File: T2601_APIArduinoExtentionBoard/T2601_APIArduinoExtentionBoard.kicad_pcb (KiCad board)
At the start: 2 copper layers, 60 x 90 mm, 75 parts, among them J1 Conn_01x10_Socket, J11 Conn_01x04_Pin, J12 Screw_Terminal_01x02, J13 Conn_01x04_Pin, J14 Screw_Terminal_01x02, J15 Conn_02x08_Counter_Clockwise, J2 Conn_01x10_Socket, J3 Conn_01x10_Socket, J4 Conn_01x10_Socket, J5 Screw_Terminal_01x08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

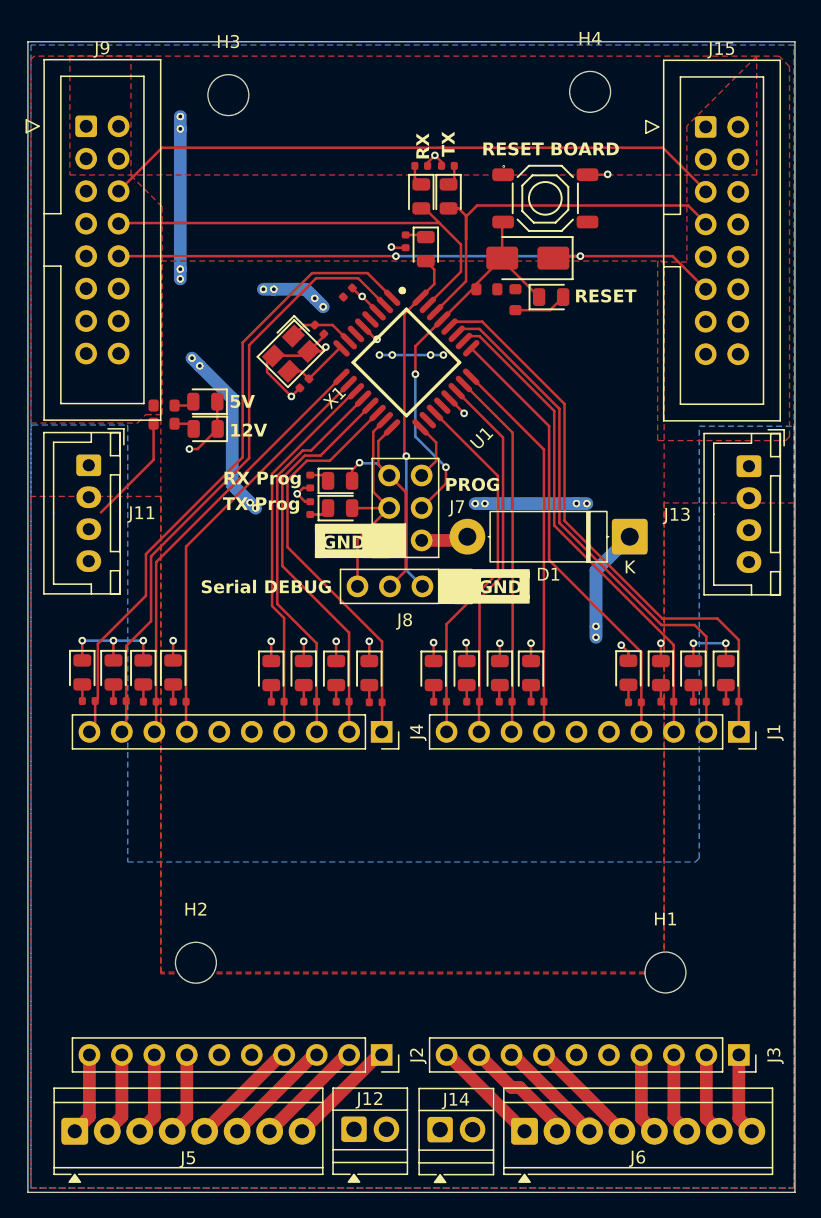
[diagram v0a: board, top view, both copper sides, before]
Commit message: V0.5 - Mounting Hole + Silkscreen
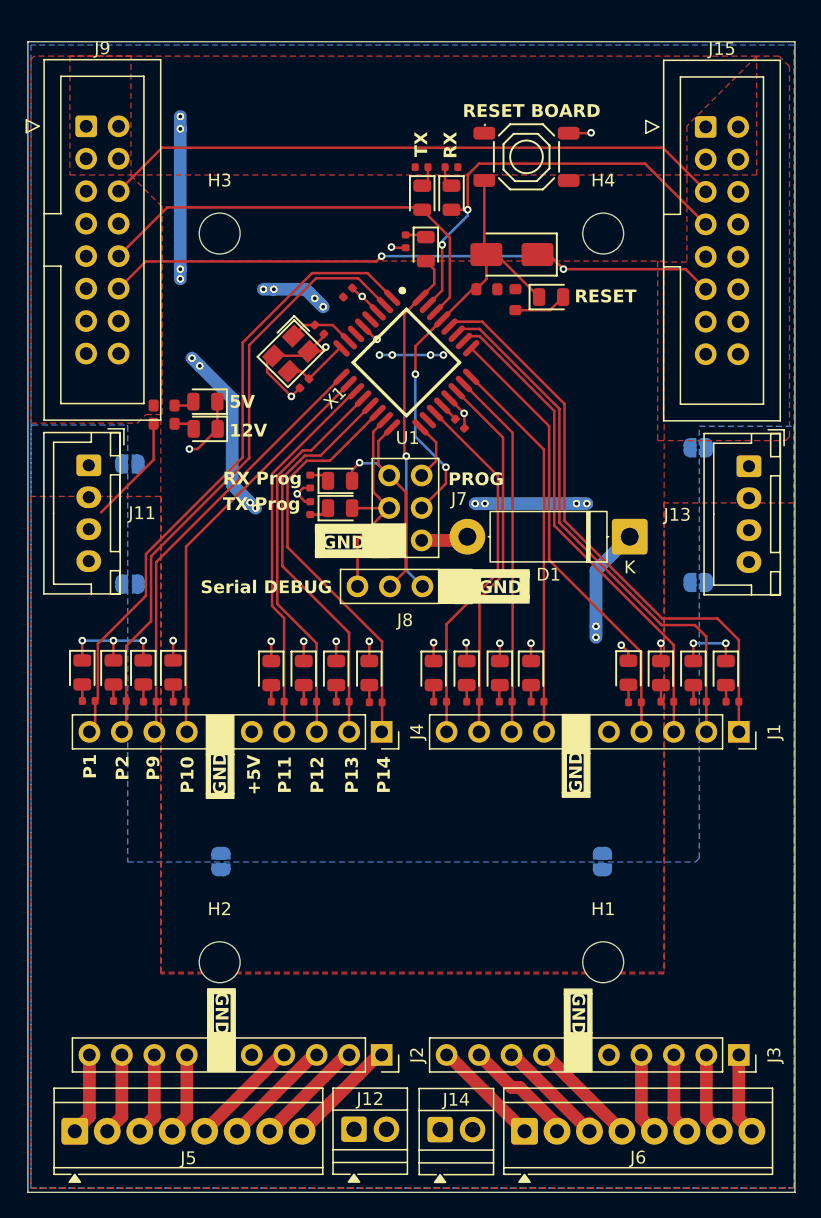
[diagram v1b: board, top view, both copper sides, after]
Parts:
- added C4: 100nF, PCM_JLCPCB:C_0402, F.Cu at (159.8, 61.9)
- added JP1: SolderJumper_2_Open, Jumper:SolderJumper-2_P1.3mm_Open_RoundedPad1.0x1.5mm, B.Cu at (178.4, 63.8)
- added JP2: SolderJumper_2_Open, Jumper:SolderJumper-2_P1.3mm_Open_RoundedPad1.0x1.5mm, B.Cu at (178.4, 74.3)
- added JP3: SolderJumper_2_Open, Jumper:SolderJumper-2_P1.3mm_Open_RoundedPad1.0x1.5mm, B.Cu at (134.0, 65.0)
- added JP4: SolderJumper_2_Open, Jumper:SolderJumper-2_P1.3mm_Open_RoundedPad1.0x1.5mm, B.Cu at (134.0, 74.4)
- added JP5: SolderJumper_2_Open, Jumper:SolderJumper-2_P1.3mm_Open_RoundedPad1.0x1.5mm, B.Cu at (141.1, 96.1)
- added JP6: SolderJumper_2_Open, Jumper:SolderJumper-2_P1.3mm_Open_RoundedPad1.0x1.5mm, B.Cu at (170.9, 96.1)
- moved H4 11.1 mm to (171.0, 47.0)
- moved H3 10.9 mm to (141.0, 47.0)
- moved H1 4.93 mm to (171.0, 104.0)
- moved S1 3.56 mm to (165.0, 41.0)
- moved D11 2.36 mm to (159.1, 44.2)
- moved R10 2.36 mm to (159.1, 41.8)
- moved D12 2.06 mm to (156.8, 44.2)
- moved R11 2.06 mm to (156.8, 41.8)
- moved H2 1.86 mm to (141.0, 104.0)
- moved D6 1.27 mm to (163.9, 48.6)
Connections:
- J15 pad 7: TX -> RX
- J9 pad 10: RX -> TX
- U1 pad 20: unconnected-(U1-AREF-Pad20) -> Net-(U1-AREF)
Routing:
- net RESET: track 31.5 -> 36.0 mm
- net TX: track 31.7 -> 34.8 mm
- net RX: track 35.2 -> 33.7 mm, vias 0 -> 2
- net Net-(U1-AREF): track 0.00 -> 1.49 mm
- net GEN_RESET: track 49.2 -> 50.6 mm
- net GND: track 60.6 -> 59.9 mm, vias 26 -> 25
- net Net-(D11-Pad1): track 1.65 -> 0.95 mm
- net Net-(D12-Pad1): track 1.63 -> 1.00 mm
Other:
- board text added: "+5V"
- board text added: "P1"
- board text added: "P10"
- board text added: "P11"
- board text added: "P12"
- board text added: "P13"
- board text added: "P14"
- board text added: "P2"
- board text added: "P9"

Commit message: Silkescreen Mod
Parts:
- added REF**: KiCad-Logo2_5mm_SilkScreen, Symbol:KiCad-Logo2_5mm_SilkScreen, F.Cu at (145.3, 36.6)
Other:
- board text added: "Copyright (C) 2026 HackHype CERN OHL-S v2"

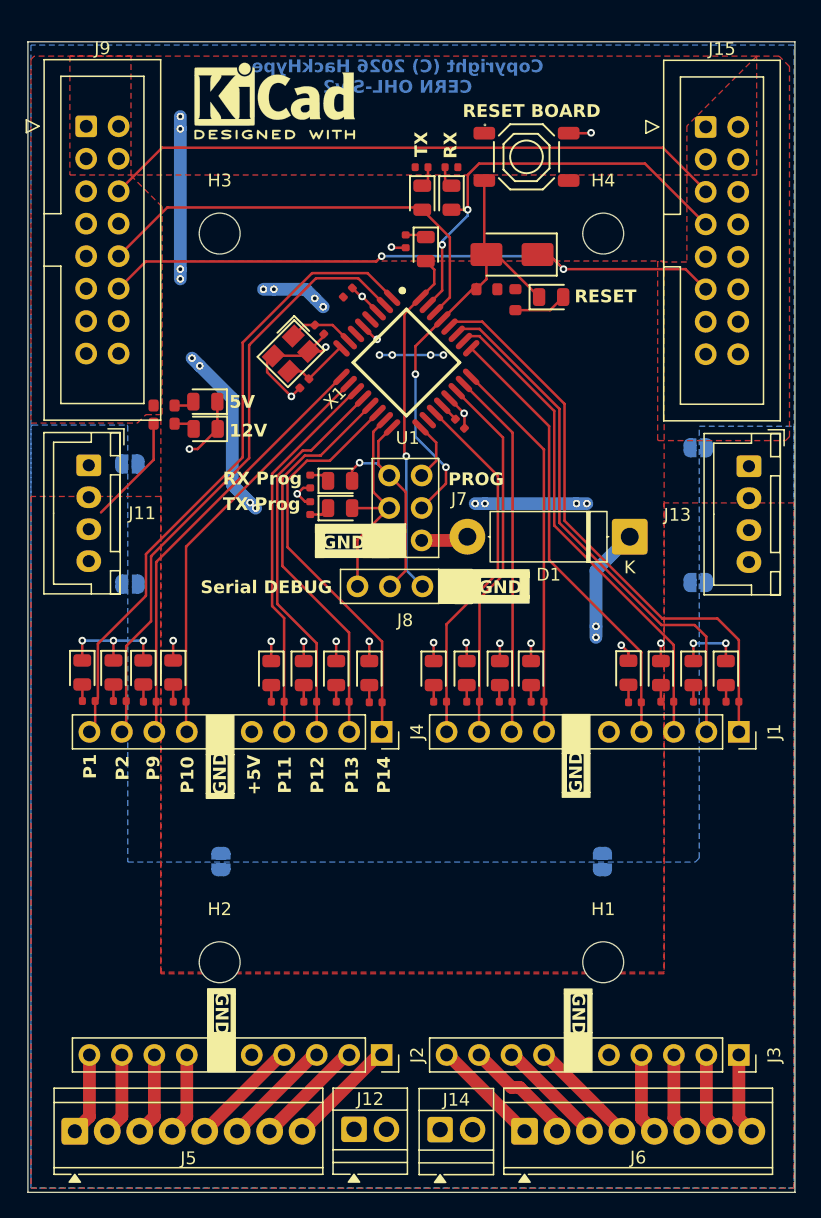
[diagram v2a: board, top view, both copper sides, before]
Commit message: Pitch Header + Silkscreen
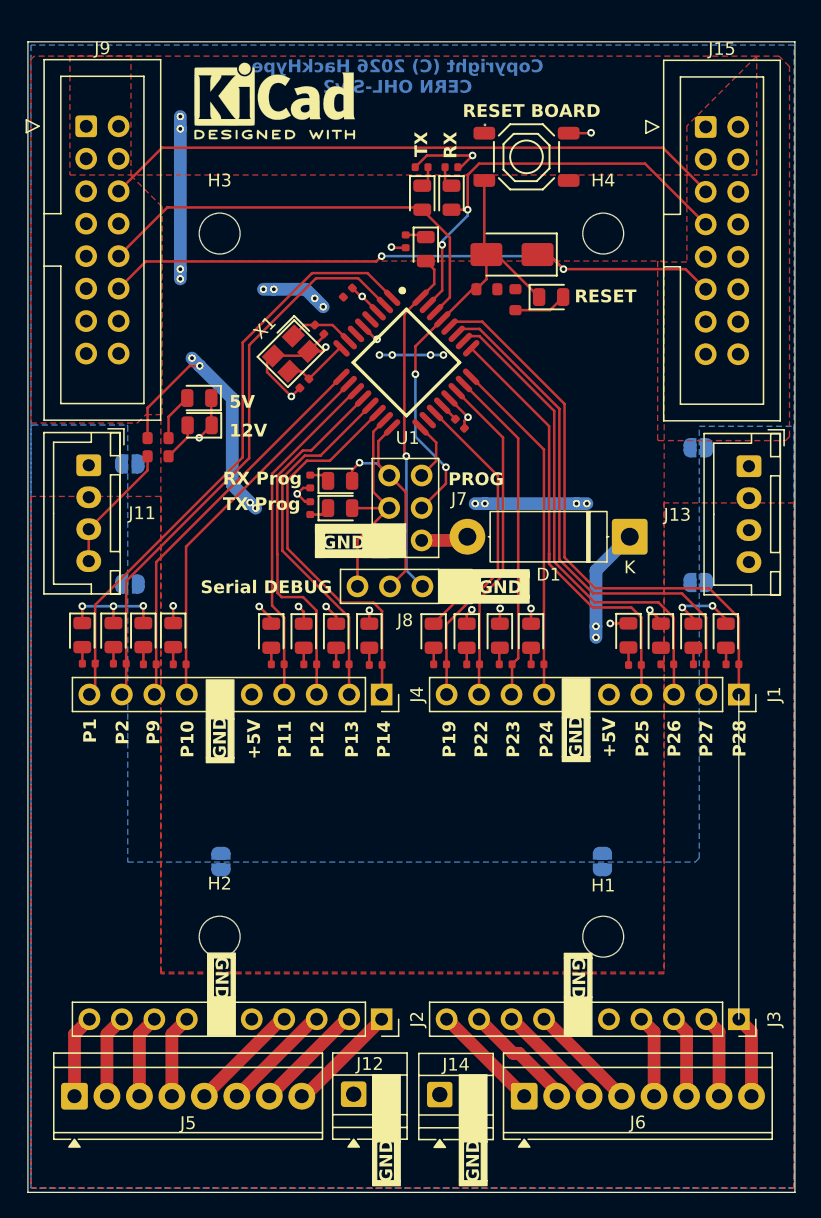
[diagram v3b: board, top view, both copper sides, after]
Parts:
- moved D15 2.92 mm to (145.0, 78.5)
- moved D16 2.92 mm to (147.6, 78.5)
- moved D17 2.92 mm to (150.1, 78.5)
- moved D18 2.92 mm to (152.7, 78.5)
- moved D19 2.92 mm to (160.3, 78.5)
- moved D2 2.92 mm to (157.7, 78.5)
- moved D20 2.92 mm to (162.9, 78.5)
- moved D21 2.92 mm to (165.4, 78.5)
- moved D22 2.92 mm to (173.0, 78.4)
- moved D23 2.92 mm to (175.5, 78.5)
- moved D24 2.92 mm to (178.1, 78.5)
- moved D25 2.92 mm to (180.6, 78.5)
- moved R1 2.92 mm to (130.8, 80.6)
- moved R2 2.92 mm to (133.2, 80.6)
- moved D14 2.92 mm to (137.4, 78.4)
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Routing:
- net +5V: track 54.4 -> 62.3 mm
- net GND: track 59.9 -> 66.3 mm
- net P2: track 48.0 -> 45.1 mm
- net P24: track 30.1 -> 27.2 mm
- net P10: track 32.5 -> 29.6 mm
- net P19: track 28.7 -> 25.7 mm
- net P9: track 34.4 -> 31.5 mm
- net P22: track 28.9 -> 26.0 mm
- net P11: track 29.8 -> 26.9 mm
- net P13: track 31.2 -> 28.4 mm
- net P1: track 50.3 -> 47.5 mm
- net P23: track 28.8 -> 26.3 mm
- net Net-(D8-Pad2): track 1.59 -> 3.74 mm
- net P12: track 30.5 -> 28.6 mm
- net +12V: track 8.64 -> 10.5 mm
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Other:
- board text added: "P19"
- board text added: "P22"
- board text added: "P23"
- board text added: "P24"
- board text added: "P25"
- board text added: "P26"
- board text added: "P27"
- board text added: "P28"

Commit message: Silkscreen/Logo/ComPin Attribution
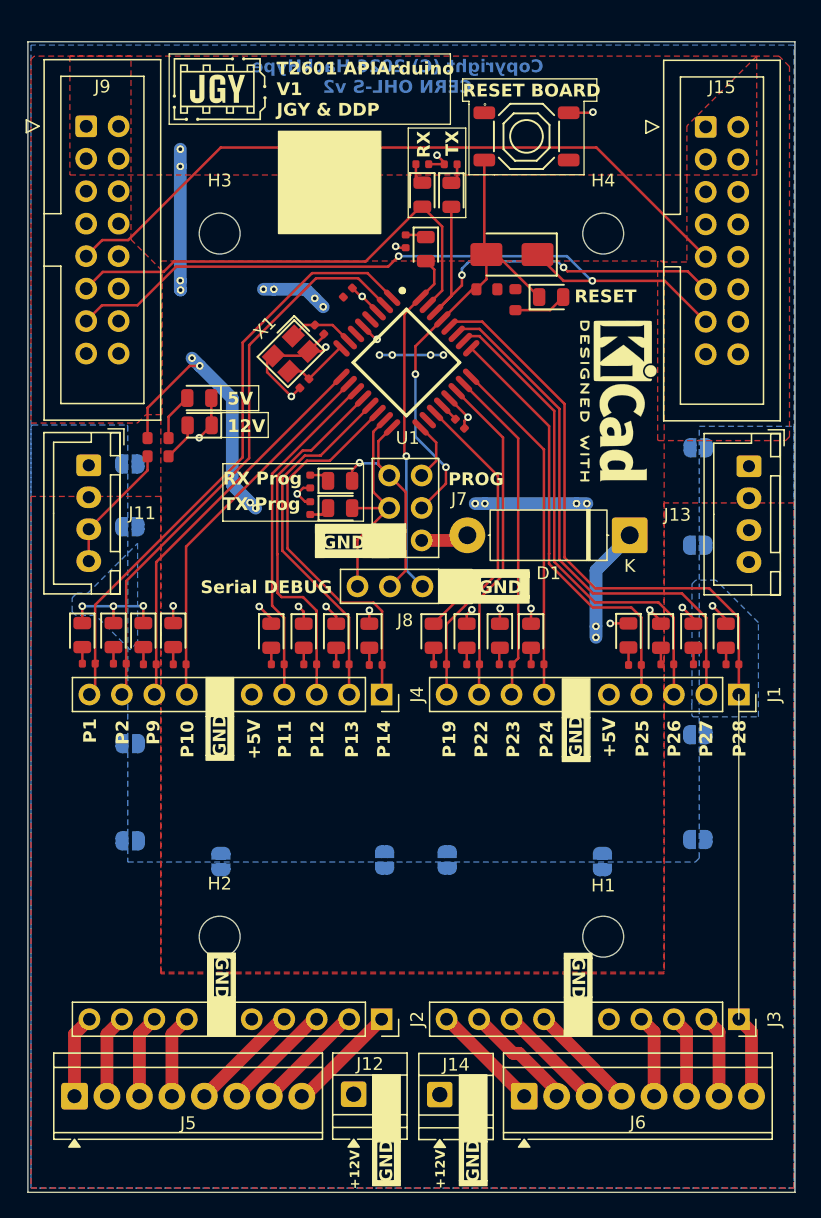
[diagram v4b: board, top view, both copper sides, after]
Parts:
- added G***: LOGO, logo.preety:logo5, F.Cu at (141.0, 35.7)
- added JP10: SolderJumper_2_Open, Jumper:SolderJumper-2_P1.3mm_Open_RoundedPad1.0x1.5mm, B.Cu at (134.0, 94.5)
- added JP11: SolderJumper_2_Open, Jumper:SolderJumper-2_P1.3mm_Open_RoundedPad1.0x1.5mm, B.Cu at (158.8, 96.0)
- added JP12: SolderJumper_2_Open, Jumper:SolderJumper-2_P1.3mm_Open_RoundedPad1.0x1.5mm, B.Cu at (153.9, 96.0)
- added JP7: SolderJumper_2_Open, Jumper:SolderJumper-2_P1.3mm_Open_RoundedPad1.0x1.5mm, B.Cu at (178.4, 86.2)
- added JP8: SolderJumper_2_Open, Jumper:SolderJumper-2_P1.3mm_Open_RoundedPad1.0x1.5mm, B.Cu at (178.4, 94.4)
- added JP9: SolderJumper_2_Open, Jumper:SolderJumper-2_P1.3mm_Open_RoundedPad1.0x1.5mm, B.Cu at (134.0, 86.9)
- moved REF** 35.7 mm to (172.2, 60.1), turned to -90 degrees
- moved JP4 4.49 mm to (134.0, 69.9)
- moved JP2 2.92 mm to (178.4, 71.4)
- moved D11 2.29 mm to (156.8, 44.0)
- moved R10 2.29 mm to (156.8, 41.6)
- moved D12 2.29 mm to (159.1, 44.0)
- moved R11 2.29 mm to (159.1, 41.6)
- moved S1 1.60 mm to (165.0, 39.4)
- moved D1 0.11 mm to (173.1, 70.6)
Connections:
- J15 pad 11: GEN_RESET -> TX
- J15 pad 13: unconnected-(J15-Pin_13-Pad13) -> GEN_RESET
- J15 pad 15: GND -> unconnected-(J15-Pin_15-Pad15)
- J15 pad 16: GND -> unconnected-(J15-Pin_16-Pad16)
- J15 pad 5: UART_BACK -> GND
- J15 pad 7: RX -> GND
- J15 pad 8: unconnected-(J15-Pin_8-Pad8) -> GND
- J15 pad 9: unconnected-(J15-Pin_9-Pad9) -> UART_BACK
- J9 pad 10: TX -> GND
- J9 pad 11: GND -> RX
- J9 pad 12: GEN_RESET -> GND
- J9 pad 13: GND -> GEN_RESET
- J9 pad 14: unconnected-(J9-Pin_14-Pad14) -> GND
- J9 pad 15: GND -> unconnected-(J9-Pin_15-Pad15)
- J9 pad 16: GND -> unconnected-(J9-Pin_16-Pad16)
- J9 pad 6: UART_BACK -> GND
- J9 pad 8: unconnected-(J9-Pin_8-Pad8) -> GND
- J9 pad 9: unconnected-(J9-Pin_9-Pad9) -> UART_BACK
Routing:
- net GEN_RESET: track 50.6 -> 57.8 mm
- net UART_BACK: track 48.8 -> 55.9 mm
- net GND: track 66.3 -> 59.5 mm
- net RX: track 33.7 -> 38.0 mm, vias 2 -> 0
- net +5V: track 62.3 -> 60.7 mm
- net TX: track 34.8 -> 33.2 mm, vias 0 -> 2
- net Net-(D23-Pad2): track 0.00 -> 1.30 mm
- net RESET: track 36.0 -> 37.1 mm
- net Net-(D11-Pad1): track 0.95 -> 1.65 mm
- net Net-(D12-Pad1): track 1.00 -> 1.63 mm
- net P25: track 34.9 -> 34.4 mm
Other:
- board text added: "+12V"
- board text added: "T2601 APIArduino V1 JGY & DDP"

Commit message: 3D models
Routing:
- net +5V: track 60.7 -> 68.0 mm, vias 22 -> 24
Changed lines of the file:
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@@
 		(at 155.6004 57.092435 -135)
 		(property "Reference" "U1"
-			(at 4.09978 -4.243464 0)
+			(at 4.318983 -4.459839 0)
 			(layer "F.SilkS")
 			(effects
@@
 		)
 		(embedded_fonts no)
-		(model "${EASYEDA2KICAD}/easyeda2kicad.3dshapes/TQFP-32_L7.0-W7.0-H1.2-LS9.0-P0.80.wrl"
+		(model "${KIPRJMOD}/M2601_APIArduinoExtentionBoard_Lib3D/TQFP-32_L7.0-W7.0-H1.2-LS9.0-P0.80.wrl"
 			(offset
 				(xyz -0 0 -0)
@@
 		)
 		(embedded_fonts no)
-		(model "${EASYEDA2KICAD}/easyeda2kicad.3dshapes/CRYSTAL-SMD_4P-L3.2-W2.5-BL.wrl"
+		(model "${KIPRJMOD}/M2601_APIArduinoExtentionBoard_Lib3D/CRYSTAL-SMD_4P-L3.2-W2.5-BL.step"
 			(offset
 				(xyz 0 -0 -0)
@@
 	)
 	(via
+		(at 164.3 54.6)
+		(size 0.6)
+		(drill 0.3)
+		(layers "F.Cu" "B.Cu")
+		(net 4)
+	)
+	(via
 		(at 137.94 51.42)
 		(size 0.6)
@@
 	)
 	(via
+		(at 165 54.6)
+		(size 0.6)
+		(drill 0.3)
+		(layers "F.Cu" "B.Cu")
+		(net 4)
+	)
+	(via
 		(at 168.91 68.1228)
 		(size 0.6)
@@
 	)
 	(segment
+		(start 164.3 54.6)
+		(end 165 54.6)
+		(width 1)
+		(layer "B.Cu")
+		(net 4)
+	)
+	(segment
+		(start 160 56.5)
+		(end 161.9 54.6)
+		(width 1)
+		(layer "B.Cu")
+		(net 4)
+	)
+	(segment
 		(start 144.4244 51.3588)
 		(end 145.2372 51.3588)
@@
 	)
 	(segment
+		(start 158.5 56.5)
+		(end 160 56.5)
+		(width 1)
+		(layer "B.Cu")
+		(net 4)
+	)
+	(segment
+		(start 161.9 54.6)
+		(end 164.3 54.6)
+		(width 1)
+		(layer "B.Cu")
+		(net 4)
+	)
+	(segment
 		(start 173.0756 70.7136)
 		(end 173.0756 70.6)
@@
 	)
 	(segment
-		(start 158.5 56.5)
-		(end 153.5 56.5)
+		(start 154.5 56.5)
+		(end 157.5 56.5)
 		(width 0.2)
 		(layer "B.Cu")
@@
 	)
 	(segment
+		(start 158.5 56.5)
+		(end 157.5 56.5)
+		(width 1)
+		(layer "B.Cu")
+		(net 4)
+	)
+	(segment
 		(start 170.434 77.724)
 		(end 170.434 73.3552)
@@
 	)
 	(segment
+		(start 153.5 56.5)
+		(end 154.5 56.5)
+		(width 0.2)
+		(layer "B.Cu")
+		(net 4)
+	)
+	(segment
 		(start 149.098 52.7304)
 		(end 148.4376 52.07)
@@
 	)
 	(segment
+		(start 156.3116 59.7)
+		(end 156.3116 55.81555)
+		(width 0.2)
+		(layer "F.Cu")
+		(net 28)
+	)
+	(segment
 		(start 161.861999 50.5764)
 		(end 161.079599 51.3588)
@@
 	)
 	(segment
+		(start 156.3116 55.81555)
+		(end 158.414685 53.712465)
+		(width 0.2)
+		(layer "F.Cu")
+		(net 28)
+	)
+	(segment
 		(start 161.861999 48.641)
 		(end 161.7 48.479001)
@@
 	)
 	(segment
-		(start 156.3116 58)
-		(end 156.3116 55.81555)
-		(width 0.2)
-		(layer "F.Cu")
-		(net 28)
-	)
-	(segment
 		(start 161.861999 48.641)
 		(end 162.6614 48.641)
@@
 	)
 	(segment
-		(start 156.3116 55.81555)
-		(end 158.414685 53.712465)
-		(width 0.2)
-		(layer "F.Cu")
-		(net 28)
-	)
-	(segment
 		(start 162.6614 48.641)
 		(end 165.9888 51.9684)
@@
 	)
 	(via
-		(at 156.3116 58)
+		(at 156.3116 59.7)
 		(size 0.6)
 		(drill 0.3)
@@
 	)
 	(segment
-		(start 156.3116 58)
+		(start 156.3116 59.7)
 		(end 156.3116 62.8904)
 		(width 0.2)
